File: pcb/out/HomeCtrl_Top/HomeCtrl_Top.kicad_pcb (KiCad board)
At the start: 2 copper layers, 65.9 x 75.2 mm, 15 parts, among them J1 B2B, J2 RJ45-A, J3 RJ45-B, J4 RJ45-C, J5 RJ45-D, J6 GPIO, U1 MCP23017, U2 DS18B20

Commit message: HomeController PRO: sterownik domowy 32 wej / 16 wyj (2 plyty, 24V)
Nowe czesci: ESP32-C3 (modul kastelowany), TJA1051 (CAN), MOV (warystor),
MOSFET mocy DPAK (TO-252). Nowe bloki: wyjscie przekaznikowe 230V, wyjscie
MOSFET DC, bank wejsc RJ45 (TVS/wejscie), RS485, CAN, ESP32-C3, zlacze TFT.

Plyta DOLNA: 24V (bezpiecznik+dioda+MOV+buck5V+LDO3V3), ekspander wyjsc,
8x przekaznik 230V + 8x MOSFET DC, kazde wlasny zacisk; przekazniki we wnetrzu.
Plyta GORNA (wezsza): ESP32-C3 + 2x ekspander (32 wejscia), 8x RJ45, RS485+CAN,
TFT dotykowy. Otwory + B2B wspolne 1:1.

Layout: I/O na krawedzi dla OBU plyt (omija otwory narozne), zaciski 230V na
dolnej krawedzi, przekazniki we wnetrzu. Heurystyka zasilania rozpoznaje V24/Vxx;
regula diod tylko dla zlacz polowych (RJ45/zaciski). Niezawodnosc: TVS na kazdym
I/O, MOV, diody gasnace, pull-down bramek, grube sciezki 230V.

Oba PCB 0/0/0, zwalidowane kiutils (140 i 77 footprintow). Testy 12/12.

Co-Authored-By: Claude Opus 4.8 (1M context) <noreply@anthropic.com>
Claude-Session: https://claude.ai/code/session_01LNGxtK2Jv1rJLBLPTwFQ9C
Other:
- board text added: "HomeCtrl_Top"
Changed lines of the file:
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@@
     (layer "Edge.Cuts")
   )
+  (gr_text
+    "HomeCtrl_Top"
+    (at 2 73.7 0)
+    (layer "F.SilkS")
+    (effects
+      (font
+        (size 1.5 1.5)
+        (thickness 0.25)
+      )
+      (justify left)
+    )
+  )
 )

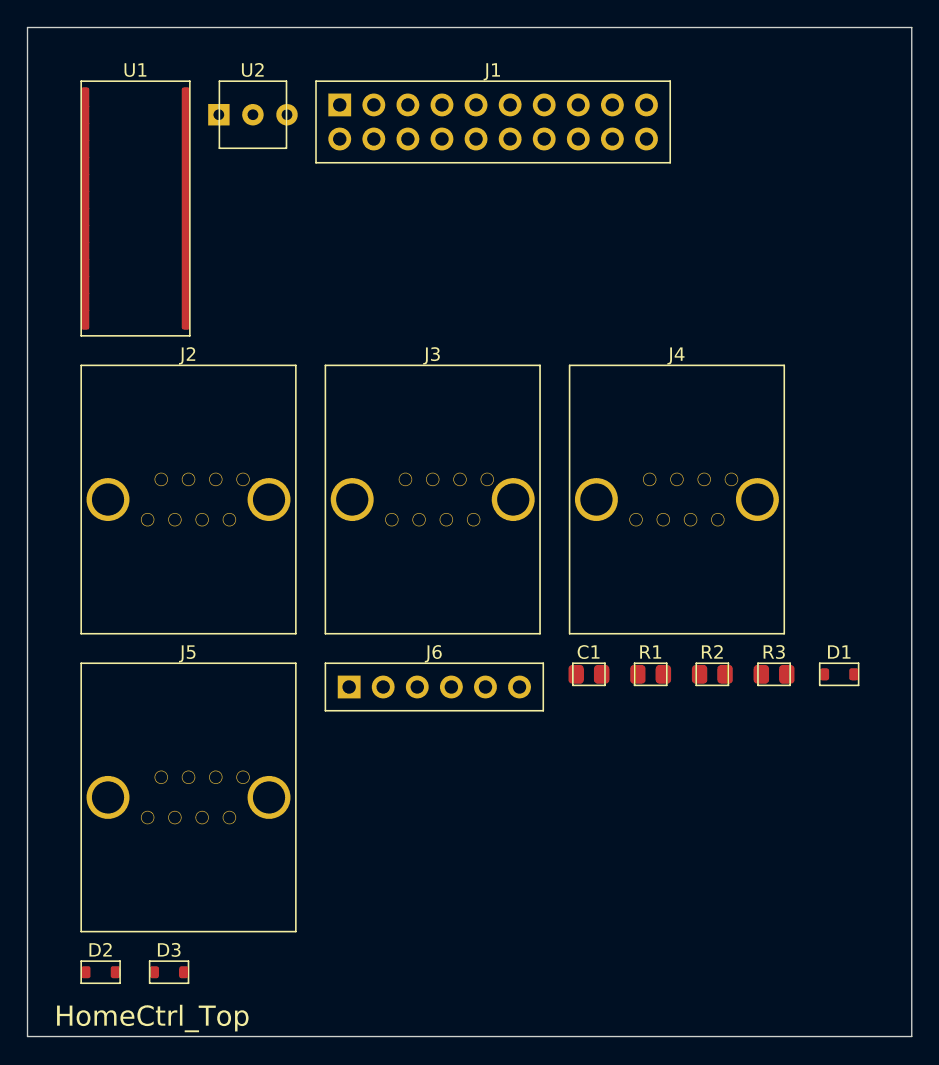
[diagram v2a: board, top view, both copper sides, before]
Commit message: ESP32-S3 + przyciski TFT; kompaktowy layout (szerokosc z liczby zlacz, 2 rzedy)
- Przejscie ESP32-C3 -> ESP32-S3 (duzo GPIO): niezalezne RS485/CAN, dotyk z IRQ,
  4 przyciski nawigacji TFT (GORA/DOL/OK/WSTECZ). Nowa czesc ESP32-S3-WROOM-1.
- Layout: I/O wzdluz krawedzi w 2 rzedach (podwojne w pionie), szerokosc plytki
  wynika z LICZBY zlacz (zmienne szerokosci kolumn) - wejscia na gornej krawedzi,
  wyjscia (zaciski) na dolnej. auto_frame() dobiera ciasna wspolna ramke.
- Przekazniki pakowane w strefe 230V (kilka rzedow) omijajaca otwory.
- HomeCtrlPro: 280x185 -> 168x192 mm, mniej pustego miejsca. Oba 0/0/0.

Testy 12/12, zwalidowane kiutils. Bloki: esp32s3, button.

Co-Authored-By: Claude Opus 4.8 (1M context) <noreply@anthropic.com>
Claude-Session: https://claude.ai/code/session_01LNGxtK2Jv1rJLBLPTwFQ9C
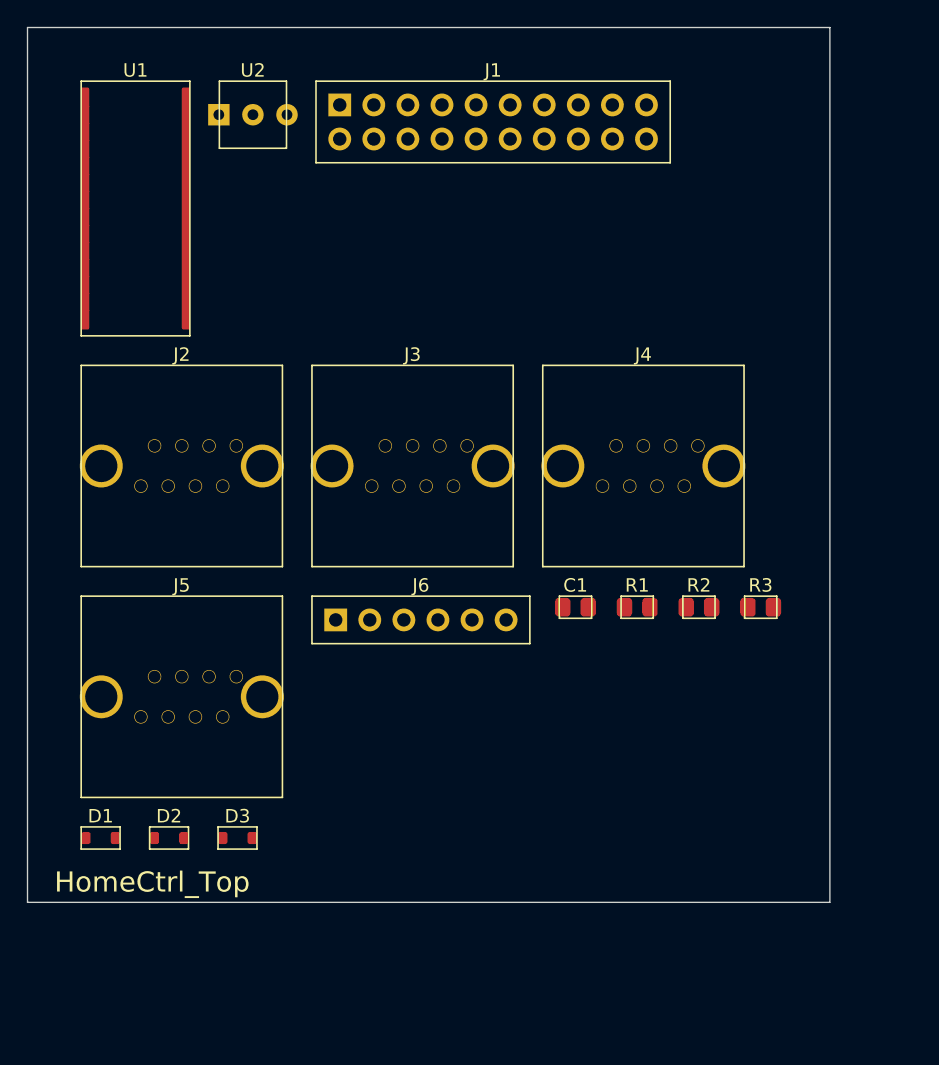
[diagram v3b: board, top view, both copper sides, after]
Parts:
- moved D1 56.4 mm to (5.45, 60.4)
- moved D2 11.2 mm to (10.6, 60.4)
- moved D3 11.2 mm to (15.7, 60.4)
- moved J5 7.52 mm to (11.5, 49.9)
- moved C1 5.10 mm to (40.8, 43.2)
- moved J6 5.10 mm to (29.3, 44.1)
- moved R1 5.10 mm to (45.4, 43.2)
- moved R2 5.10 mm to (50.0, 43.2)
- moved R3 5.10 mm to (54.6, 43.2)
- moved J4 3.54 mm to (45.9, 32.7)
- moved J3 2.92 mm to (28.7, 32.7)
- moved J2 2.55 mm to (11.5, 32.7)
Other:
- board size 65.9 x 75.2 mm -> 59.8 x 65.2 mm
